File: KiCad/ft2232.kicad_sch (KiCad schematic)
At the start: 34 parts, among them J801 USB_C_Receptacle_USB2.0_16P, U801 FT2232HQ, U802 93LCxxB, Y801 12MHz

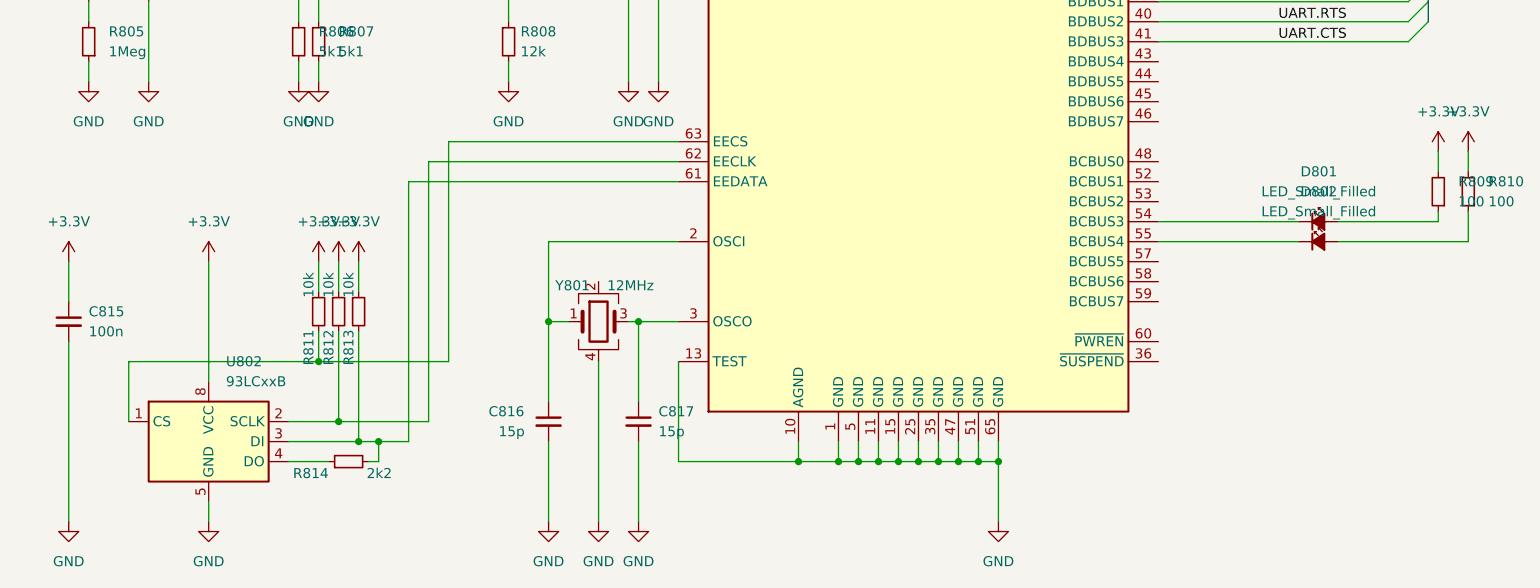
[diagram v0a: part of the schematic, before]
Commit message: replaced SAR-ADC with Sigma-Delta-Converter
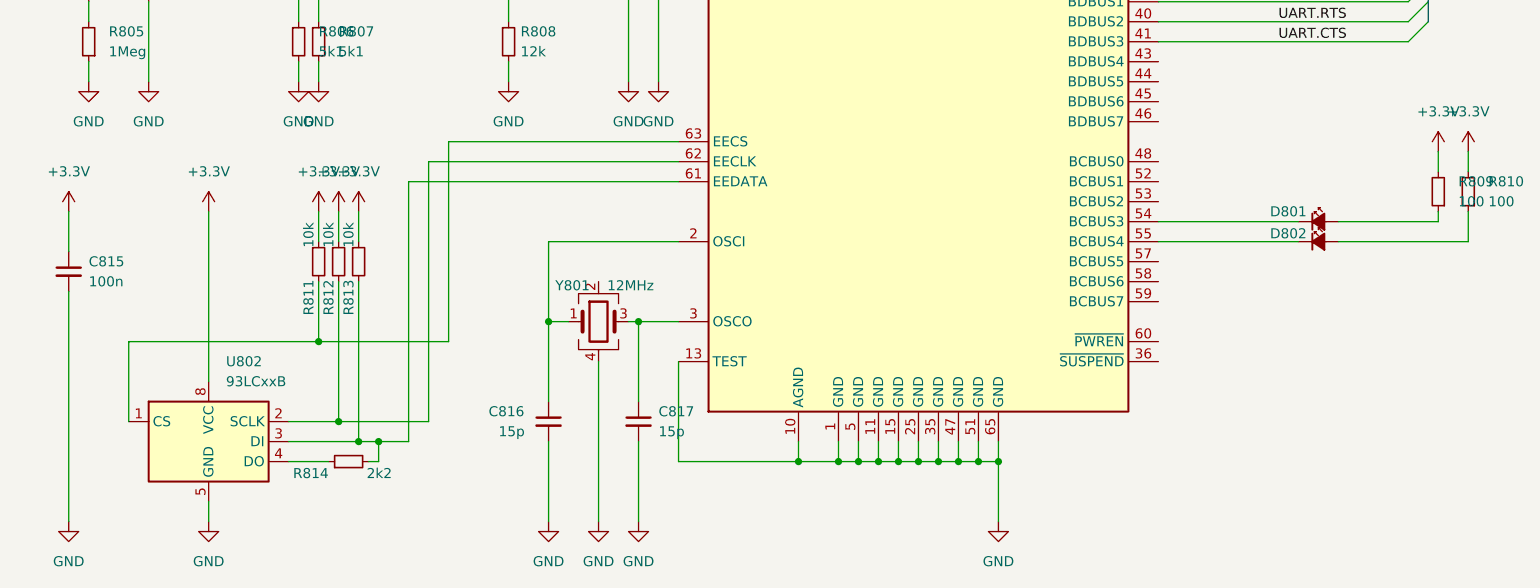
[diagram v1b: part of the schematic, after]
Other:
- moved on the sheet: C815, R811, R812, R813

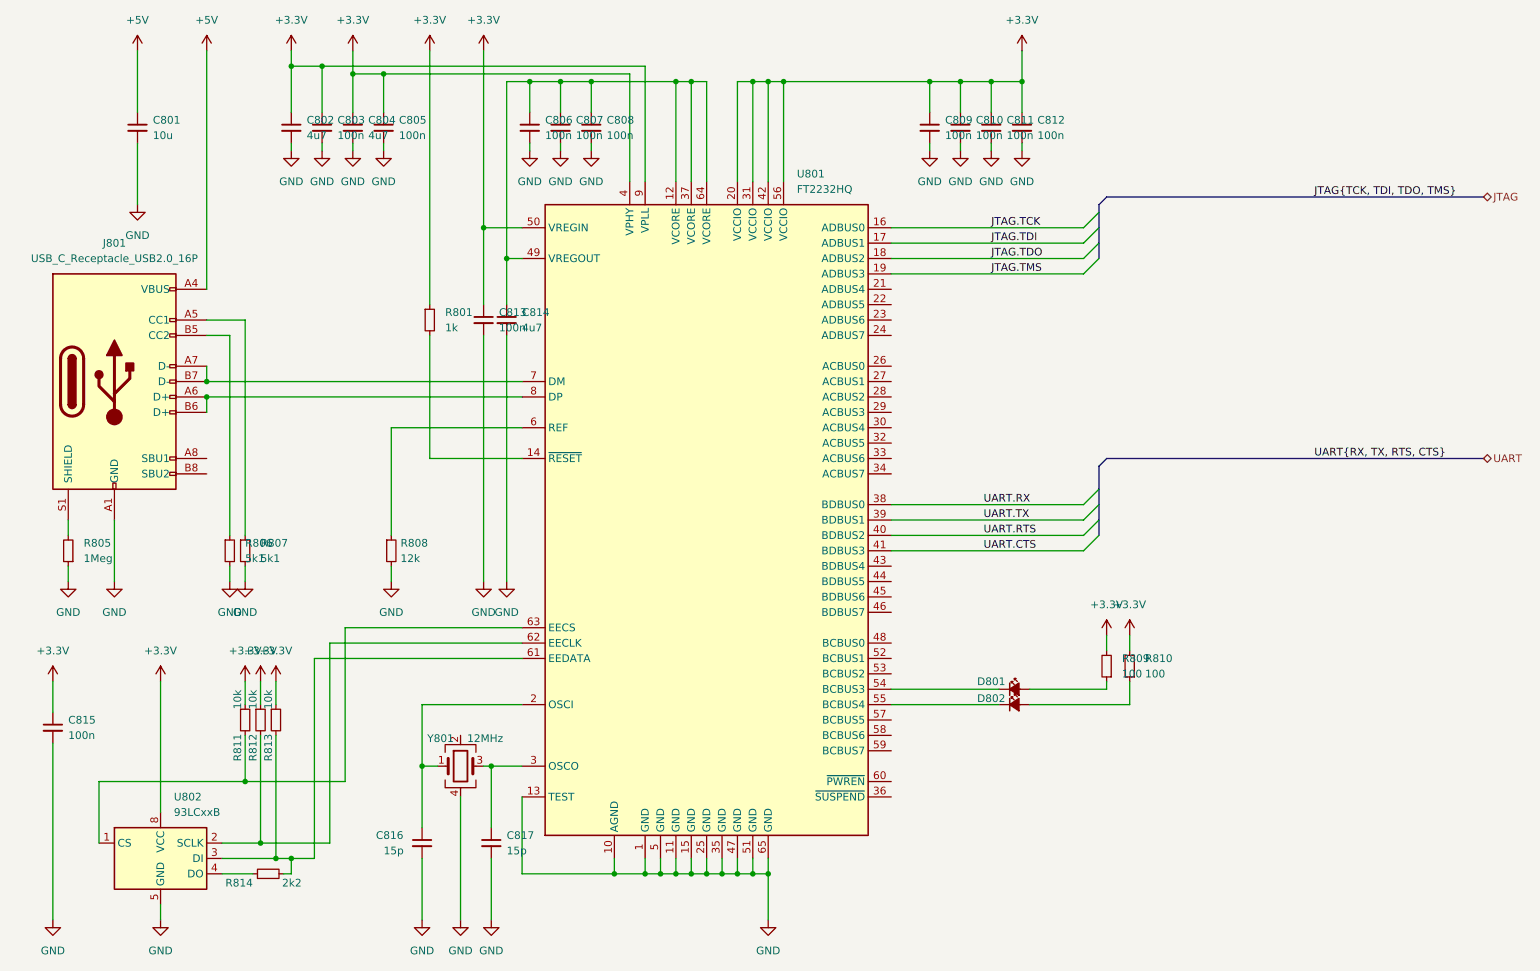
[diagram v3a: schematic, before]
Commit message: LEDs zur Visualisierung des ausgewählten FPGAs
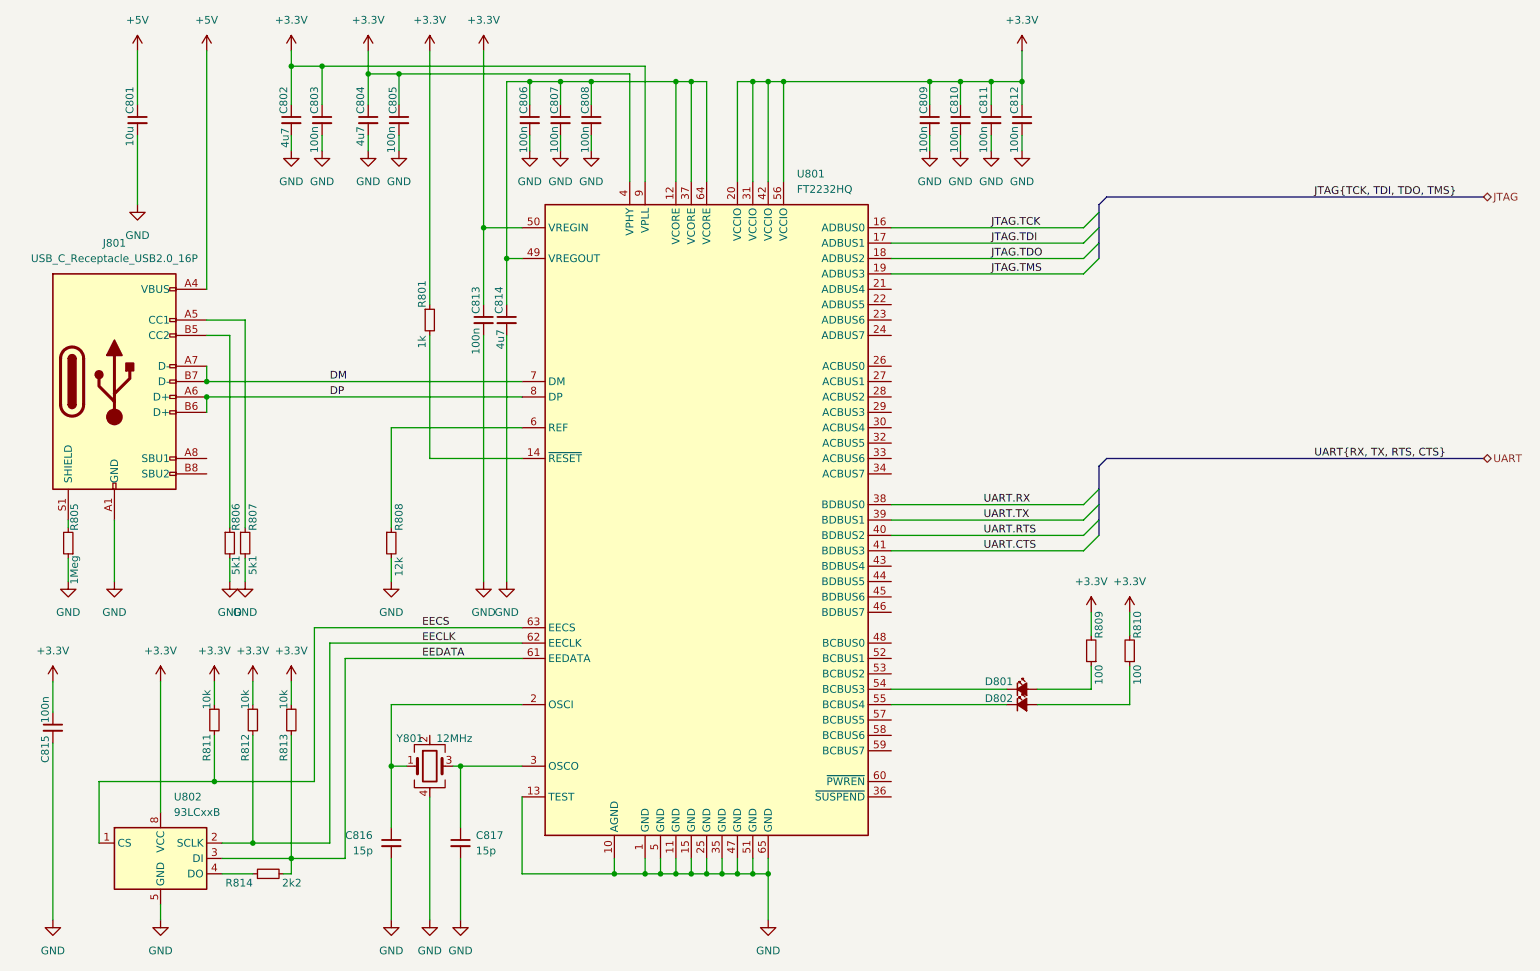
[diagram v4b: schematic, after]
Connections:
- net EEDATA: now reaches R813.2, R814.2, U801.61 (EEDATA), U802.3 (DI)
- net EECLK: now reaches R812.2, U801.62 (EECLK), U802.2 (SCLK)
- net EECS: now reaches R811.2, U801.63 (EECS), U802.1 (CS)
- net DM: now reaches J801.A7 (D-), J801.B7 (D-), U801.7 (DM)
- net DP: now reaches J801.A6 (D+), J801.B6 (D+), U801.8 (DP)
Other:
- moved on the sheet: C801, C802, C803, C804, C805, C806, C807, C808, C809, C810, C811, C812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
